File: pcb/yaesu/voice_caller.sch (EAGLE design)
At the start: 56 parts, among them IC1 78L12SMD, IC2 LM386M-1, IC3 25F32006WSOI

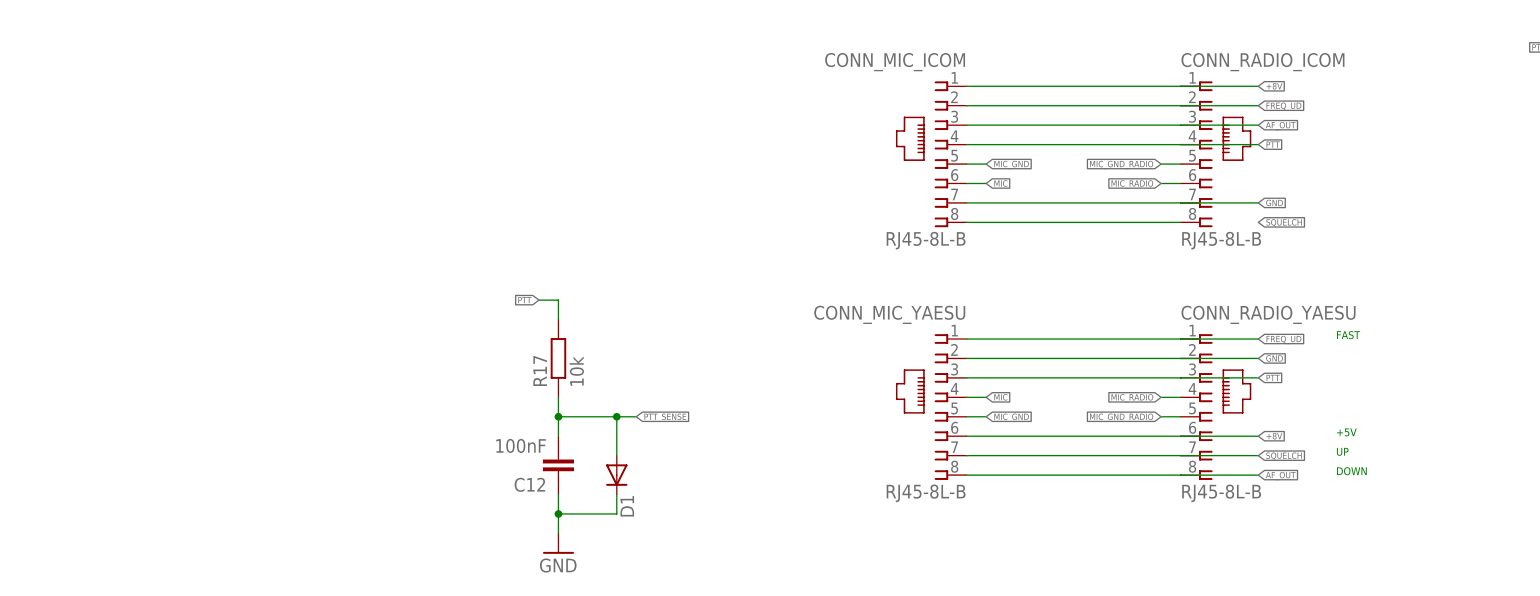
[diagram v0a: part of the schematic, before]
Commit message: Connector connections corredted.
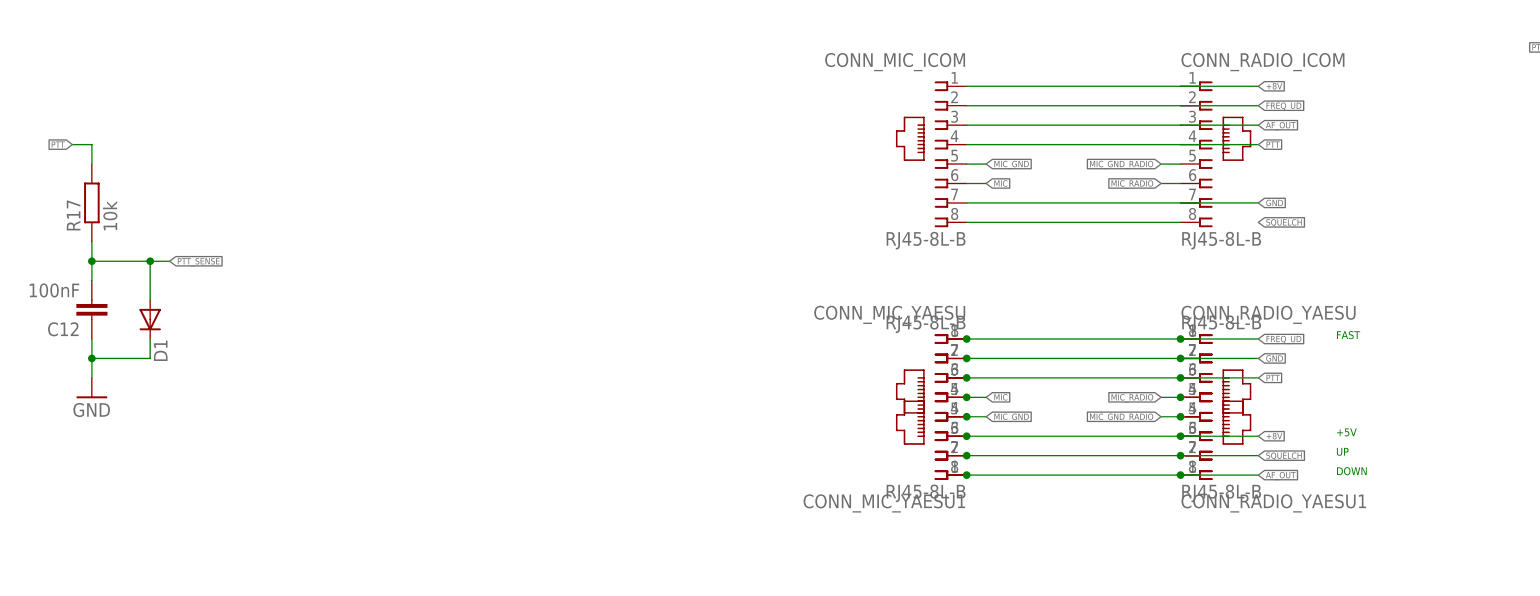
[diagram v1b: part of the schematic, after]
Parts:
- added CONN_MIC_YAESU1, CONN_RADIO_YAESU1: RJ45-8L-B, con-tycoelectronics:RJ45-8L-B
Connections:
- net +8V: now also CONN_MIC_YAESU1.3, CONN_RADIO_YAESU1.3
- net AF_OUT: now also CONN_MIC_YAESU1.1, CONN_RADIO_YAESU1.1
- net FREQ_UD: now also CONN_MIC_YAESU1.8, CONN_RADIO_YAESU1.8
- net GND: now also CONN_MIC_YAESU1.7, CONN_RADIO_YAESU1.7
- net MIC: now also CONN_MIC_YAESU1.5
- net MIC_GND: now also CONN_MIC_YAESU1.4
- net MIC_GND_RADIO: now also CONN_RADIO_YAESU1.4
- net MIC_RADIO: now also CONN_RADIO_YAESU1.5
- net PTT: now also CONN_MIC_YAESU1.6, CONN_RADIO_YAESU1.6
- net SQUELCH: now also CONN_MIC_YAESU1.2, CONN_RADIO_YAESU1.2
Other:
- moved on the sheet: C12, D1, R17
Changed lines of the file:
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@@
 <part name="CONN_RADIO_YAESU" library="con-tycoelectronics" deviceset="RJ45" device="" technology="-8L-B"/>
 <part name="R18" library="rcl" deviceset="R-EU_" device="M1206" value="0R_Yaesu"/>
+<part name="CONN_MIC_YAESU1" library="con-tycoelectronics" deviceset="RJ45" device="" technology="-8L-B"/>
+<part name="CONN_RADIO_YAESU1" library="con-tycoelectronics" deviceset="RJ45" device="" technology="-8L-B"/>
 </parts>
 <sheets>
@@
 <instance part="GND26" gate="1" x="-68.58" y="91.44"/>
 <instance part="C4" gate="G$1" x="-68.58" y="106.68"/>
-<instance part="R17" gate="G$1" x="-81.28" y="22.86" rot="R90"/>
-<instance part="C12" gate="G$1" x="-81.28" y="7.62" rot="R180"/>
-<instance part="D1" gate="G$1" x="-73.66" y="7.62" rot="R270"/>
-<instance part="GND27" gate="1" x="-81.28" y="-2.54"/>
+<instance part="R17" gate="G$1" x="-142.24" y="43.18" rot="R90"/>
+<instance part="C12" gate="G$1" x="-142.24" y="27.94" rot="R180"/>
+<instance part="D1" gate="G$1" x="-134.62" y="27.94" rot="R270"/>
+<instance part="GND27" gate="1" x="-142.24" y="17.78"/>
 <instance part="C13" gate="G$1" x="-15.24" y="99.06"/>
 <instance part="C14" gate="G$1" x="5.08" y="99.06"/>
@@
 <instance part="CONN_RADIO_YAESU" gate="G$1" x="2.54" y="17.78"/>
 <instance part="R18" gate="G$1" x="154.94" y="127"/>
+<instance part="CONN_MIC_YAESU1" gate="G$1" x="-30.48" y="15.24" rot="R180"/>
+<instance part="CONN_RADIO_YAESU1" gate="G$1" x="2.54" y="15.24" rot="MR180"/>
 </instances>
 <busses>
@@
 <segment>
 <pinref part="C12" gate="G$1" pin="1"/>
-<wire x1="-81.28" y1="5.08" x2="-81.28" y2="2.54" width="0.1524" layer="91"/>
-<wire x1="-81.28" y1="2.54" x2="-73.66" y2="2.54" width="0.1524" layer="91"/>
+<wire x1="-142.24" y1="25.4" x2="-142.24" y2="22.86" width="0.1524" layer="91"/>
+<wire x1="-142.24" y1="22.86" x2="-134.62" y2="22.86" width="0.1524" layer="91"/>
 <pinref part="D1" gate="G$1" pin="C"/>
-<wire x1="-73.66" y1="2.54" x2="-73.66" y2="5.08" width="0.1524" layer="91"/>
+<wire x1="-134.62" y1="22.86" x2="-134.62" y2="25.4" width="0.1524" layer="91"/>
 <pinref part="GND27" gate="1" pin="GND"/>
-<wire x1="-81.28" y1="0" x2="-81.28" y2="2.54" width="0.1524" layer="91"/>
-<junction x="-81.28" y="2.54"/>
+<wire x1="-142.24" y1="20.32" x2="-142.24" y2="22.86" width="0.1524" layer="91"/>
+<junction x="-142.24" y="22.86"/>
 </segment>
 <segment>
@@
 <wire x1="0" y1="22.86" x2="10.16" y2="22.86" width="0.1524" layer="91"/>
 <label x="10.16" y="22.86" size="0.8128" layer="95" xref="yes"/>
+<pinref part="CONN_MIC_YAESU1" gate="G$1" pin="7"/>
+<junction x="-27.94" y="22.86"/>
+<pinref part="CONN_RADIO_YAESU1" gate="G$1" pin="7"/>
+<junction x="0" y="22.86"/>
 </segment>
 </net>
@@
 <segment>
 <pinref part="R17" gate="G$1" pin="2"/>
-<wire x1="-81.28" y1="27.94" x2="-81.28" y2="30.48" width="0.1524" layer="91"/>
-<wire x1="-81.28" y1="30.48" x2="-83.82" y2="30.48" width="0.1524" layer="91"/>
-<label x="-83.82" y="30.48" size="0.8128" layer="95" rot="R180" xref="yes"/>
+<wire x1="-142.24" y1="48.26" x2="-142.24" y2="50.8" width="0.1524" layer="91"/>
+<wire x1="-142.24" y1="50.8" x2="-144.78" y2="50.8" width="0.1524" layer="91"/>
+<label x="-144.78" y="50.8" size="0.8128" layer="95" rot="R180" xref="yes"/>
 </segment>
 <segment>
@@
 <wire x1="0" y1="20.32" x2="10.16" y2="20.32" width="0.1524" layer="91"/>
 <label x="10.16" y="20.32" size="0.8128" layer="95" xref="yes"/>
+<pinref part="CONN_MIC_YAESU1" gate="G$1" pin="6"/>
+<junction x="-27.94" y="20.32"/>
+<pinref part="CONN_RADIO_YAESU1" gate="G$1" pin="6"/>
+<junction x="0" y="20.32"/>
 </segment>
 </net>
@@
 <wire x1="0" y1="12.7" x2="10.16" y2="12.7" width="0.1524" layer="91"/>
 <label x="10.16" y="12.7" size="0.8128" layer="95" xref="yes"/>
+<pinref part="CONN_MIC_YAESU1" gate="G$1" pin="3"/>
+<junction x="-27.94" y="12.7"/>
+<pinref part="CONN_RADIO_YAESU1" gate="G$1" pin="3"/>
+<junction x="0" y="12.7"/>
 </segment>
 </net>
@@
 <wire x1="0" y1="25.4" x2="10.16" y2="25.4" width="0.1524" layer="91"/>
 <label x="10.16" y="25.4" size="0.8128" layer="95" xref="yes"/>
+<pinref part="CONN_MIC_YAESU1" gate="G$1" pin="8"/>
+<junction x="-27.94" y="25.4"/>
+<pinref part="CONN_RADIO_YAESU1" gate="G$1" pin="8"/>
+<junction x="0" y="25.4"/>
 </segment>
 </net>
@@
 <wire x1="0" y1="10.16" x2="10.16" y2="10.16" width="0.1524" layer="91"/>
 <label x="10.16" y="10.16" size="0.8128" layer="95" xref="yes"/>
+<pinref part="CONN_MIC_YAESU1" gate="G$1" pin="2"/>
+<junction x="-27.94" y="10.16"/>
+<pinref part="CONN_RADIO_YAESU1" gate="G$1" pin="2"/>
+<junction x="0" y="10.16"/>
 </segment>
 </net>
@@
 <wire x1="0" y1="15.24" x2="-2.54" y2="15.24" width="0.1524" layer="91"/>
 <label x="-2.54" y="15.24" size="0.8128" layer="95" rot="R180" xref="yes"/>
+<pinref part="CONN_RADIO_YAESU1" gate="G$1" pin="4"/>
+<junction x="0" y="15.24"/>
 </segment>
 </net>
@@
 <wire x1="0" y1="7.62" x2="10.16" y2="7.62" width="0.1524" layer="91"/>
 <label x="10.16" y="7.62" size="0.8128" layer="95" xref="yes"/>
+<pinref part="CONN_MIC_YAESU1" gate="G$1" pin="1"/>
+<junction x="-27.94" y="7.62"/>
+<pinref part="CONN_RADIO_YAESU1" gate="G$1" pin="1"/>
+<junction x="0" y="7.62"/>
 </segment>
 </net>
@@
 <wire x1="-27.94" y1="17.78" x2="-25.4" y2="17.78" width="0.1524" layer="91"/>
 <label x="-25.4" y="17.78" size="0.8128" layer="95" xref="yes"/>
+<pinref part="CONN_MIC_YAESU1" gate="G$1" pin="5"/>
+<junction x="-27.94" y="17.78"/>
 </segment>
 </net>
@@
 <wire x1="0" y1="17.78" x2="-2.54" y2="17.78" width="0.1524" layer="91"/>
 <label x="-2.54" y="17.78" size="0.8128" layer="95" rot="R180" xref="yes"/>
+<pinref part="CONN_RADIO_YAESU1" gate="G$1" pin="5"/>
+<junction x="0" y="17.78"/>
 </segment>
 </net>
@@
 <wire x1="-27.94" y1="15.24" x2="-25.4" y2="15.24" width="0.1524" layer="91"/>
 <label x="-25.4" y="15.24" size="0.8128" layer="95" xref="yes"/>
+<pinref part="CONN_MIC_YAESU1" gate="G$1" pin="4"/>
+<junction x="-27.94" y="15.24"/>
 </segment>
 </net>
@@
 <segment>
 <pinref part="R17" gate="G$1" pin="1"/>
-<wire x1="-81.28" y1="17.78" x2="-81.28" y2="15.24" width="0.1524" layer="91"/>
+<wire x1="-142.24" y1="38.1" x2="-142.24" y2="35.56" width="0.1524" layer="91"/>
 <pinref part="C12" gate="G$1" pin="2"/>
-<wire x1="-81.28" y1="15.24" x2="-81.28" y2="12.7" width="0.1524" layer="91"/>
-<wire x1="-81.28" y1="15.24" x2="-73.66" y2="15.24" width="0.1524" layer="91"/>
+<wire x1="-142.24" y1="35.56" x2="-142.24" y2="33.02" width="0.1524" layer="91"/>
+<wire x1="-142.24" y1="35.56" x2="-134.62" y2="35.56" width="0.1524" layer="91"/>
 <pinref part="D1" gate="G$1" pin="A"/>
-<wire x1="-73.66" y1="15.24" x2="-73.66" y2="10.16" width="0.1524" layer="91"/>
-<junction x="-81.28" y="15.24"/>
-<wire x1="-73.66" y1="15.24" x2="-71.12" y2="15.24" width="0.1524" layer="91"/>
-<junction x="-73.66" y="15.24"/>
-<label x="-71.12" y="15.24" size="0.8128" layer="95" xref="yes"/>
-</segment>
-</net>
+<wire x1="-134.62" y1="35.56" x2="-134.62" y2="30.48" width="0.1524" layer="91"/>
+<junction x="-142.24" y="35.56"/>
+<wire x1="-134.62" y1="35.56" x2="-132.08" y2="35.56" width="0.1524" layer="91"/>
+<junction x="-134.62" y="35.56"/>
+<label x="-132.08" y="35.56" size="0.8128" layer="95" xref="yes"/>
+</segment>
+</net>
